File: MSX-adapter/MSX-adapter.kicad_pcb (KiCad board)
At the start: 2 copper layers, 65.5 x 24.5 mm, 2 parts, among them J1 MSX_BUS, J2 Bus_ISA_8bit

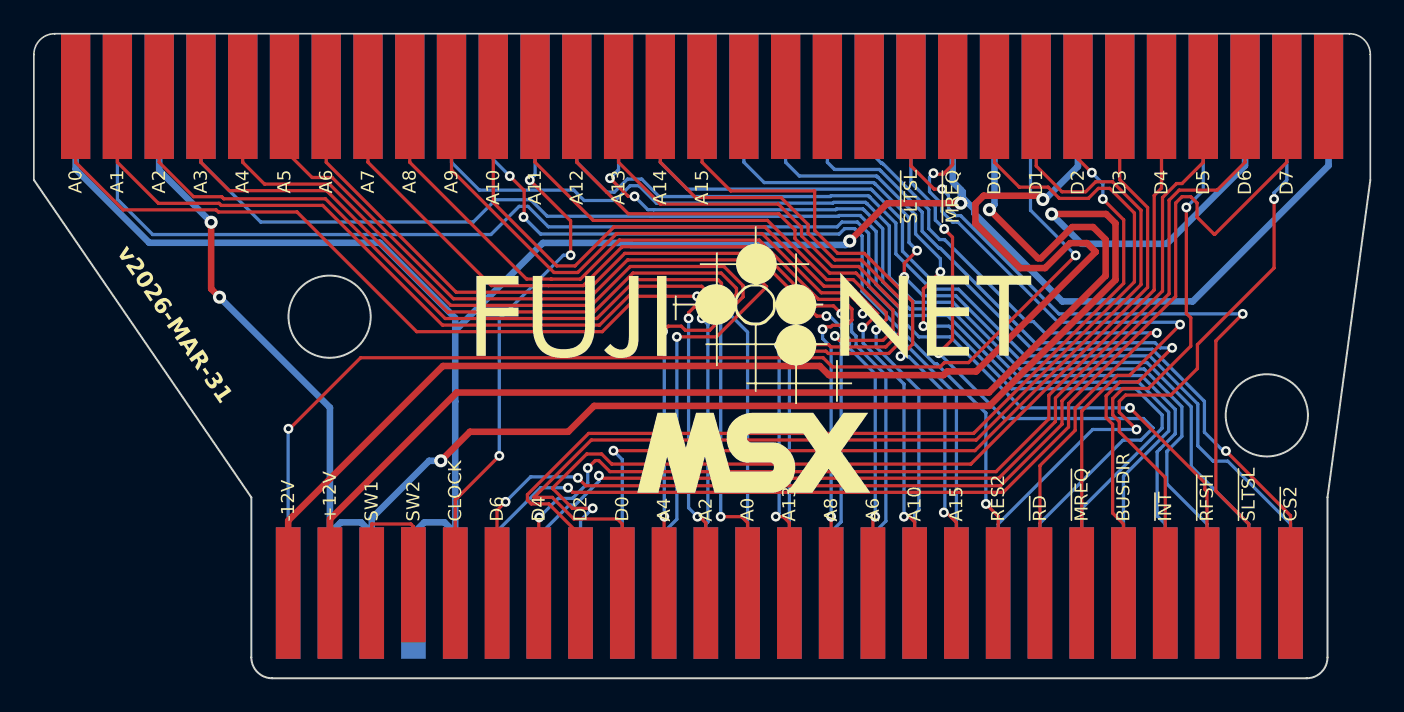
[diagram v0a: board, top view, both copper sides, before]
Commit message: Fix edge cuts and labels
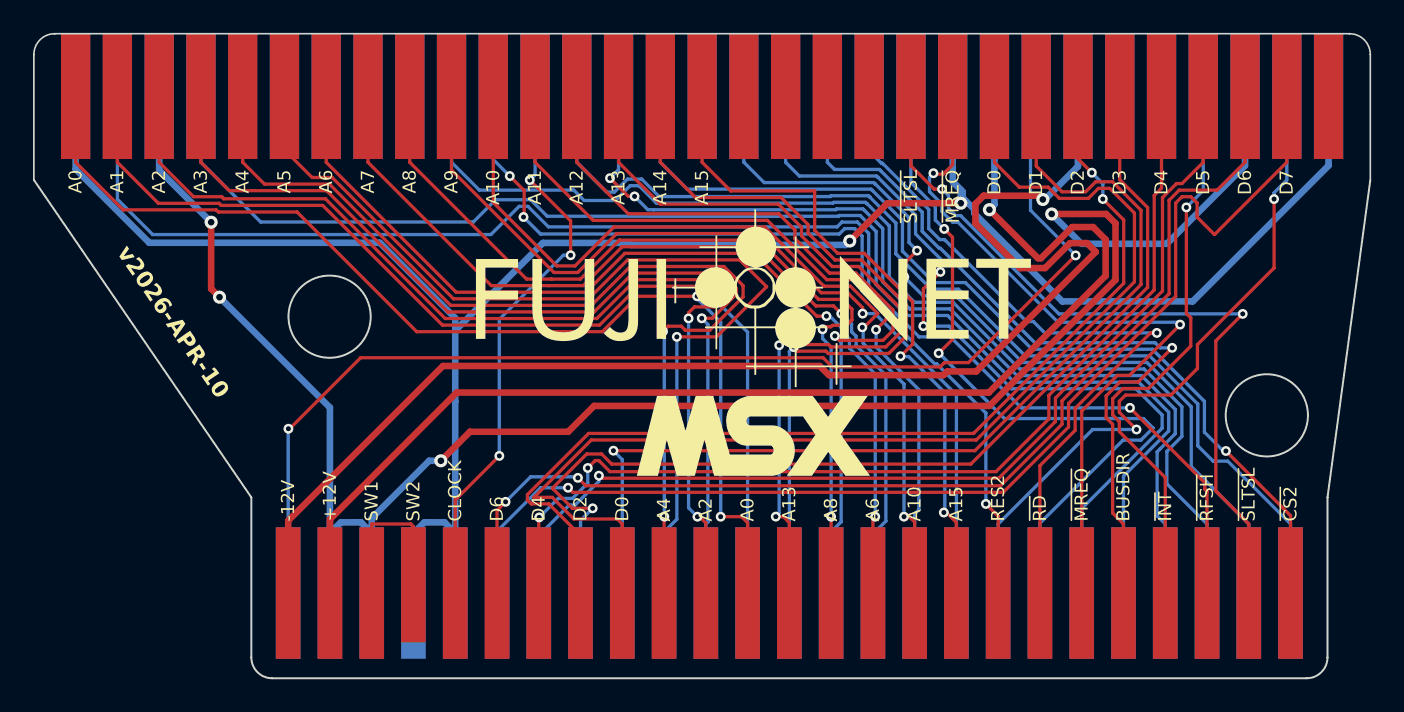
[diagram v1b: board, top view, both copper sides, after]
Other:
- board text added: "v2026-APR-10"
- board text removed: "v2026-MAR-31"
- board text removed: "~{IOEQ}"
